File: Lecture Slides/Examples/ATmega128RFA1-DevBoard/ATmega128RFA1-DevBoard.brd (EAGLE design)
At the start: 57.1 x 53.3 mm, 51 parts, among them J1 ISP, J2 ARDUINO_UNO_R3, J3 POWER_JACKPTH_LOCK, U1 ATMEGA128RFA1, U2 LM1117, Y1 16MHz, Y2 32.768kHz

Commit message: update slides
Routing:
- net 3.3V: track 158.5 -> 0.00 mm, vias 7 -> 0
- net RESET: track 125.2 -> 0.00 mm, vias 2 -> 0
- net RX0: track 104.2 -> 0.00 mm, vias 2 -> 0
- net TX0: track 94.2 -> 0.00 mm, vias 2 -> 0
- net MOSI: track 90.7 -> 0.00 mm
- net MISO: track 88.0 -> 0.00 mm
- net SCK: track 85.4 -> 0.00 mm, vias 1 -> 0
- net AREF: track 83.9 -> 0.00 mm
- net PE3: track 61.6 -> 0.00 mm, vias 2 -> 0
- net PB5: track 61.5 -> 0.00 mm
- net PE4: track 58.6 -> 0.00 mm, vias 2 -> 0
- net GND: track 58.2 -> 0.00 mm, vias 33 -> 0
- net VCC: track 56.5 -> 0.00 mm, vias 2 -> 0
- net PB4: track 55.8 -> 0.00 mm
- net PE5: track 55.8 -> 0.00 mm, vias 2 -> 0
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
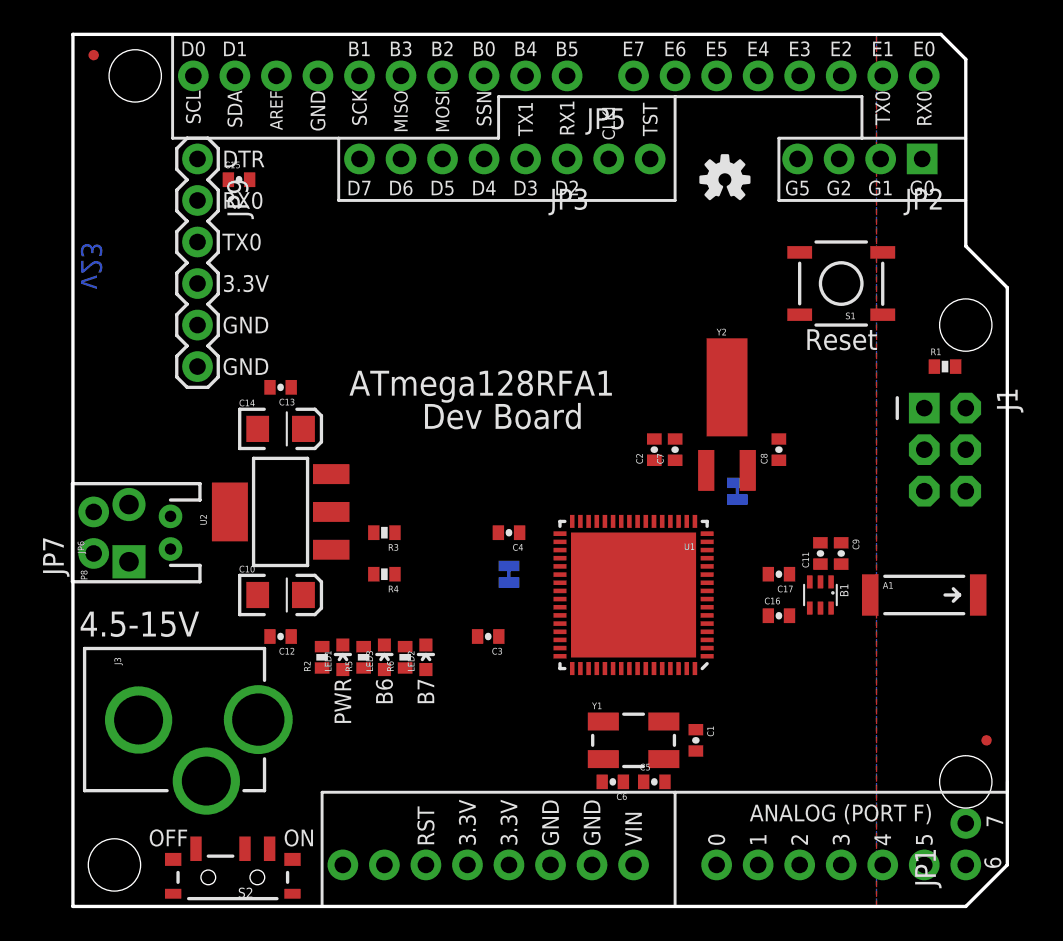
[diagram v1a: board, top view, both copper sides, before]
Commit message: examples for board layout/placement
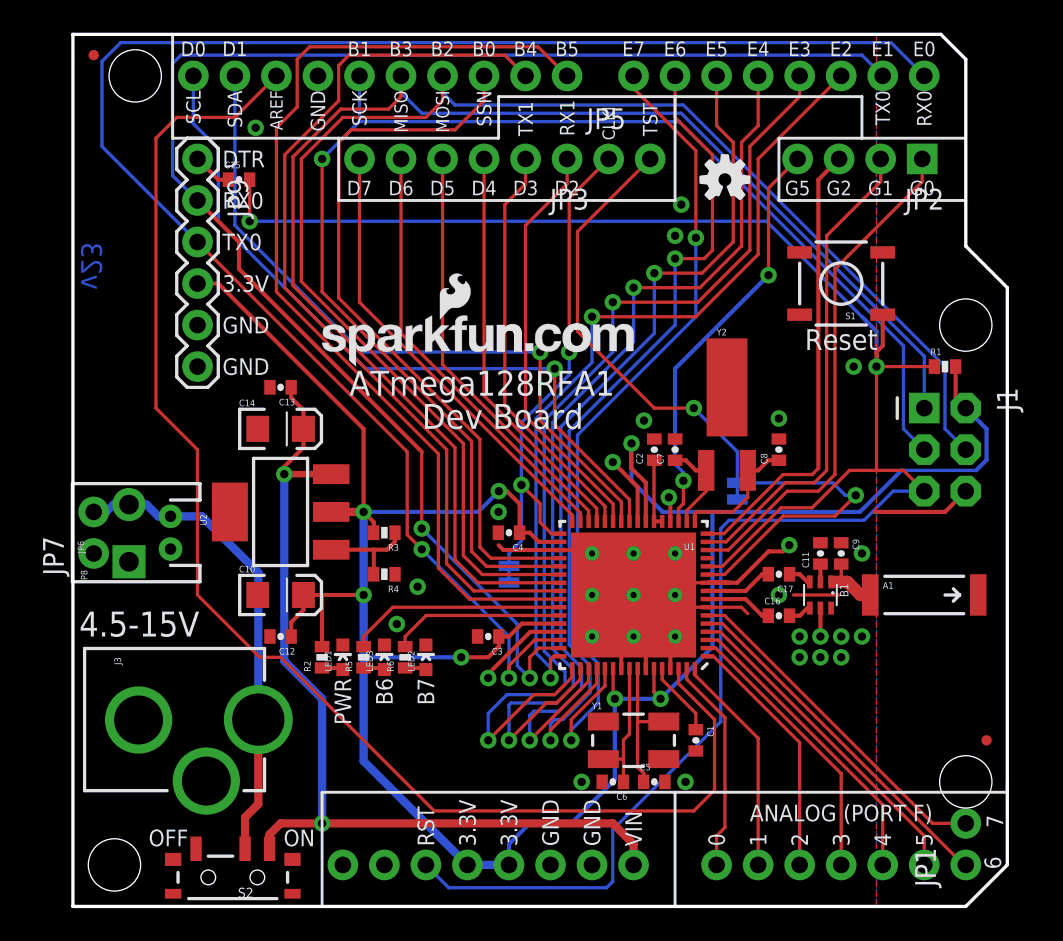
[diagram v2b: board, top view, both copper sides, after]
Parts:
- added JP10: LOGO-SFENEW, SparkFun-Aesthetics:SFE-NEW-WEBLOGO
- A1: device ATmega128RFA1-DevBoard:ANTENNA-CHIP5 -> SparkFun-RF:ANTENNA-CHIP5
- B1: device ATmega128RFA1-DevBoard:BALUN -> SparkFun-RF:BALUN
- C1, C11, C12, C13, C15, C2, C3, C4, C5, C6, C7, C8, C9: device ATmega128RFA1-DevBoard:0402-CAP -> SparkFun-Passives:0402-CAP
- C10, C14: device ATmega128RFA1-DevBoard:EIA3216 -> SparkFun-Passives:EIA3216
- C16, C17: device ATmega128RFA1-DevBoard:0402-CAP -> SparkFun:0402-CAP
- FID1, FID2: device ATmega128RFA1-DevBoard:MICRO-FIDUCIAL -> SparkFun-Aesthetics:MICRO-FIDUCIAL
- J1: device ATmega128RFA1-DevBoard:2X3-NS -> SparkFun-Connectors:2X3-NS
- J2: device ATmega128RFA1-DevBoard:ARDUINO_UNO_R3 -> SparkFun-Boards:ARDUINO_UNO_R3
- J3: device ATmega128RFA1-DevBoard:POWER_JACK_PTH_LOCK -> SparkFun-Connectors:POWER_JACK_PTH_LOCK
- JP1, JP5, JP7: device ATmega128RFA1-DevBoard:1X02_NO_SILK -> SparkFun-Connectors:1X02_NO_SILK
- JP2: device ATmega128RFA1-DevBoard:1X04_NO_SILK -> SparkFun-Connectors:1X04_NO_SILK
- JP3: device ATmega128RFA1-DevBoard:1X06_NS -> SparkFun-Connectors:1X06_NS
- JP4: device ATmega128RFA1-DevBoard:SFE-NEW-WEBLOGO -> SparkFun-Aesthetics:SFE-NEW-WEBLOGO
- JP6: device ATmega128RFA1-DevBoard:JST-2-PTH -> SparkFun-Connectors:JST-2-PTH
- JP8: device ATmega128RFA1-DevBoard:SCREWTERMINAL-3.5MM-2-NS -> SparkFun-Connectors:SCREWTERMINAL-3.5MM-2-NS
- JP9: device ATmega128RFA1-DevBoard:FTDI_BASIC -> SparkFun-Connectors:FTDI_BASIC
- LED1, LED2, LED3: device ATmega128RFA1-DevBoard:LED-0603 -> SparkFun-LED:LED-0603
- R1, R2: device ATmega128RFA1-DevBoard:0402-RES -> SparkFun-Passives:0402-RES
- R3, R4, R5, R6: device ATmega128RFA1-DevBoard:0402-RES -> SparkFun:0402-RES
- S1: device ATmega128RFA1-DevBoard:TACTILE_SWITCH_SMD -> SparkFun-Electromechanical:TACTILE_SWITCH_SMD
- S2: device ATmega128RFA1-DevBoard:SWITCH-SPST-SMD-A -> SparkFun:SWITCH-SPST-SMD-A
- SJ1, SJ2: device ATmega128RFA1-DevBoard:SJ_2S-TRACE -> SparkFun-Passives:SJ_2S-TRACE
- U$1: device ATmega128RFA1-DevBoard:OSHW-LOGO-S -> SparkFun-Aesthetics:OSHW-LOGO-S
- U1: device ATmega128RFA1-DevBoard:QFN-64 -> SparkFun-DigitalIC:QFN-64
- U2: device ATmega128RFA1-DevBoard:SOT223 -> SparkFun:SOT223
- Y1: device ATmega128RFA1-DevBoard:CRYSTAL-SMD-5X3 -> SparkFun-FreqCtrl:CRYSTAL-SMD-5X3
- Y2: device ATmega128RFA1-DevBoard:CRYSTAL-32KHZ-SMD -> SparkFun-FreqCtrl:CRYSTAL-32KHZ-SMD
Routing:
- net 3.3V: track 0.00 -> 158.5 mm, vias 0 -> 7
- net RESET: track 0.00 -> 125.2 mm, vias 0 -> 2
- net RX0: track 0.00 -> 104.2 mm, vias 0 -> 2
- net TX0: track 0.00 -> 94.2 mm, vias 0 -> 2
- net MOSI: track 0.00 -> 90.7 mm
- net MISO: track 0.00 -> 88.0 mm
- net SCK: track 0.00 -> 85.4 mm, vias 0 -> 1
- net AREF: track 0.00 -> 83.9 mm
- net PE3: track 0.00 -> 61.6 mm, vias 0 -> 2
- net PB5: track 0.00 -> 61.5 mm
- net PE4: track 0.00 -> 58.6 mm, vias 0 -> 2
- net GND: track 0.00 -> 58.2 mm, vias 0 -> 33
- net VCC: track 0.00 -> 56.5 mm, vias 0 -> 2
- net PB4: track 0.00 -> 55.8 mm
- net PE5: track 0.00 -> 55.8 mm, vias 0 -> 2
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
